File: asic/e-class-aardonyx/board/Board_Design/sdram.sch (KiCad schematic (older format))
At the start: 30 parts, among them J4 Conn_1x4, U15 SKT32E, U2 IS42S32160F-TSOP2, U3 CDCE913PW, Y2 27MHz

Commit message: updated compo placement
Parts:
- TP3, TP4: footprint TestPoint:TestPoint_Bridge_Pitch2.54mm_Drill0.7mm -> Connector_PinHeader_2.54mm:PinHeader_1x01_P2.54mm_Vertical
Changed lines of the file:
@@
 F 0 "TP3" V 10250 2888 50  0000 L CNN
 F 1 "TestPoint" V 10295 2888 50  0001 L CNN
-F 2 "TestPoint:TestPoint_Bridge_Pitch2.54mm_Drill0.7mm" H 10450 2700 50  0001 C CNN
+F 2 "Connector_PinHeader_2.54mm:PinHeader_1x01_P2.54mm_Vertical" H 10450 2700 50  0001 C CNN
 F 3 "~" H 10450 2700 50  0001 C CNN
 	1    10250 2700
@@
 F 0 "TP4" V 10250 2988 50  0000 L CNN
 F 1 "TestPoint" V 10295 2988 50  0001 L CNN
-F 2 "TestPoint:TestPoint_Bridge_Pitch2.54mm_Drill0.7mm" H 10450 2800 50  0001 C CNN
+F 2 "Connector_PinHeader_2.54mm:PinHeader_1x01_P2.54mm_Vertical" H 10450 2800 50  0001 C CNN
 F 3 "~" H 10450 2800 50  0001 C CNN
 	1    10250 2800

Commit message: add bom
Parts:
- R19, R20, R21, R22, R23: Digikey PartNumber 311-4.7KJRTR-ND -> 311-4.7KJRCT-ND
- U3: Description IC PROG PLL VCXO CLK SYN 14TSSOP -> IC PROG PLL VCXO CLK SYN 14TSSOP; Maufaturer Texas Instruments -> Texas Instruments
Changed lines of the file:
@@
 F 1 "4.7KE, 0402" V 7050 1900 50  0000 L CNN
 F 2 "Resistor_SMD:R_0402_1005Metric" V 7190 2190 50  0001 C CNN
-F 3 "https://www.digikey.in/product-detail/en/yageo/RC0402JR-074K7L/311-4-7KJRTR-ND/726477" H 7150 2200 50  0001 C CNN
+F 3 "https://www.digikey.in/product-detail/en/yageo/RC0402JR-074K7L/311-4-7KJRCT-ND/726477" H 7150 2200 50  0001 C CNN
 F 4 "RES SMD 4.7K OHM 5% 1/16W 0402" H 7150 2200 50  0001 C CNN "Description"
-F 5 "311-4.7KJRTR-ND" H 7150 2200 50  0001 C CNN "Digikey PartNumber"
+F 5 "311-4.7KJRCT-ND" H 7150 2200 50  0001 C CNN "Digikey PartNumber"
 F 6 "RC0402JR-074K7L" H 7150 2200 50  0001 C CNN "Manufactured Part Number"
 F 7 "Yageo" H 7150 2200 50  0001 C CNN "Maufaturer"
@@
 F 1 "4.7KE, 0402" V 6750 1900 50  0000 L CNN
 F 2 "Resistor_SMD:R_0402_1005Metric" V 6890 2190 50  0001 C CNN
-F 3 "https://www.digikey.in/product-detail/en/yageo/RC0402JR-074K7L/311-4-7KJRTR-ND/726477" H 6850 2200 50  0001 C CNN
+F 3 "https://www.digikey.in/product-detail/en/yageo/RC0402JR-074K7L/311-4-7KJRCT-ND/726477" H 6850 2200 50  0001 C CNN
 F 4 "RES SMD 4.7K OHM 5% 1/16W 0402" H 6850 2200 50  0001 C CNN "Description"
-F 5 "311-4.7KJRTR-ND" H 6850 2200 50  0001 C CNN "Digikey PartNumber"
+F 5 "311-4.7KJRCT-ND" H 6850 2200 50  0001 C CNN "Digikey PartNumber"
 F 6 "RC0402JR-074K7L" H 6850 2200 50  0001 C CNN "Manufactured Part Number"
 F 7 "Yageo" H 6850 2200 50  0001 C CNN "Maufaturer"
@@
 F 1 "4.7KE, 0402" V 7300 1900 50  0000 L CNN
 F 2 "Resistor_SMD:R_0402_1005Metric" V 7440 2190 50  0001 C CNN
-F 3 "https://www.digikey.in/product-detail/en/yageo/RC0402JR-074K7L/311-4-7KJRTR-ND/726477" H 7400 2200 50  0001 C CNN
+F 3 "https://www.digikey.in/product-detail/en/yageo/RC0402JR-074K7L/311-4-7KJRCT-ND/726477" H 7400 2200 50  0001 C CNN
 F 4 "RES SMD 4.7K OHM 5% 1/16W 0402" H 7400 2200 50  0001 C CNN "Description"
-F 5 "311-4.7KJRTR-ND" H 7400 2200 50  0001 C CNN "Digikey PartNumber"
+F 5 "311-4.7KJRCT-ND" H 7400 2200 50  0001 C CNN "Digikey PartNumber"
 F 6 "RC0402JR-074K7L" H 7400 2200 50  0001 C CNN "Manufactured Part Number"
 F 7 "Yageo" H 7400 2200 50  0001 C CNN "Maufaturer"
@@
 F 1 "4.7KE, 0402" H 7650 2700 50  0000 L CNN
 F 2 "Resistor_SMD:R_0402_1005Metric" V 7690 2790 50  0001 C CNN
-F 3 "https://www.digikey.in/product-detail/en/yageo/RC0402JR-074K7L/311-4-7KJRTR-ND/726477" H 7650 2800 50  0001 C CNN
+F 3 "https://www.digikey.in/product-detail/en/yageo/RC0402JR-074K7L/311-4-7KJRCT-ND/726477" H 7650 2800 50  0001 C CNN
 F 4 "NA" H 7750 2800 50  0000 C CNN "Field4"
 F 5 "RES SMD 4.7K OHM 5% 1/16W 0402" H 7650 2800 50  0001 C CNN "Description"
-F 6 "311-4.7KJRTR-ND" H 7650 2800 50  0001 C CNN "Digikey PartNumber"
+F 6 "311-4.7KJRCT-ND" H 7650 2800 50  0001 C CNN "Digikey PartNumber"
 F 7 "RC0402JR-074K7L" H 7650 2800 50  0001 C CNN "Manufactured Part Number"
 F 8 "Yageo" H 7650 2800 50  0001 C CNN "Maufaturer"
@@
 F 1 "4.7KE, 0402" H 7700 1950 50  0000 L CNN
 F 2 "Resistor_SMD:R_0402_1005Metric" V 7690 1990 50  0001 C CNN
-F 3 "https://www.digikey.in/product-detail/en/yageo/RC0402JR-074K7L/311-4-7KJRTR-ND/726477" H 7650 2000 50  0001 C CNN
+F 3 "https://www.digikey.in/product-detail/en/yageo/RC0402JR-074K7L/311-4-7KJRCT-ND/726477" H 7650 2000 50  0001 C CNN
 F 4 "NA" H 7750 2050 50  0000 C CNN "Field4"
 F 5 "RES SMD 4.7K OHM 5% 1/16W 0402" H 7650 2000 50  0001 C CNN "Description"
-F 6 "311-4.7KJRTR-ND" H 7650 2000 50  0001 C CNN "Digikey PartNumber"
+F 6 "311-4.7KJRCT-ND" H 7650 2000 50  0001 C CNN "Digikey PartNumber"
 F 7 "RC0402JR-074K7L" H 7650 2000 50  0001 C CNN "Manufactured Part Number"
 F 8 "Yageo" H 7650 2000 50  0001 C CNN "Maufaturer"
@@
 F 6 "Texas Instruments" H 8750 2200 50  0001 L BNN "Field6"
 F 7 "1543748" H 8750 2200 50  0001 L BNN "Field7"
-F 8 "	IC PROG PLL VCXO CLK SYN 14TSSOP" H 8750 2200 50  0001 C CNN "Description"
+F 8 "IC PROG PLL VCXO CLK SYN 14TSSOP" H 8750 2200 50  0001 C CNN "Description"
 F 9 "296-38908-1-ND" H 8750 2200 50  0001 C CNN "Digikey PartNumber"
 F 10 "CDCE913PWR" H 8750 2200 50  0001 C CNN "Manufactured Part Number"
-F 11 "	Texas Instruments" H 8750 2200 50  0001 C CNN "Maufaturer"
+F 11 "Texas Instruments" H 8750 2200 50  0001 C CNN "Maufaturer"
 	1    8750 2200
 	1    0    0    -1

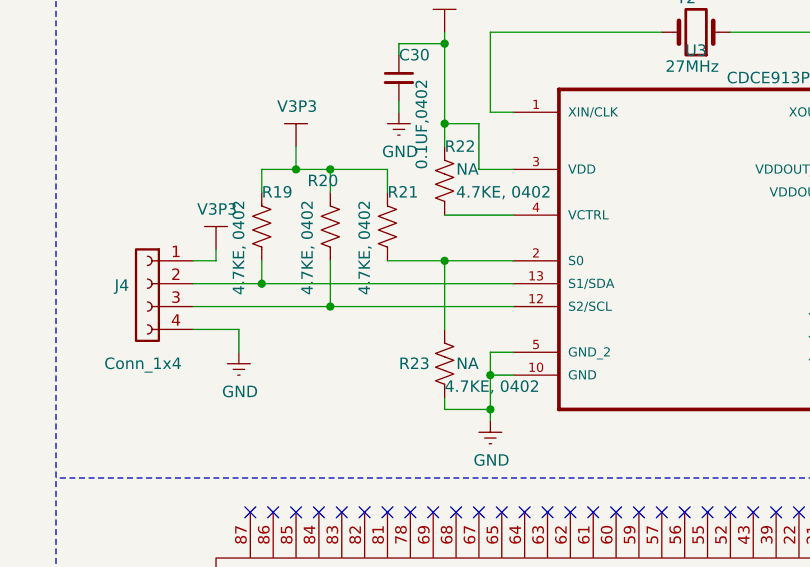
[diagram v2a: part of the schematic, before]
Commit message: Replacing ADM1085 with ADM1186
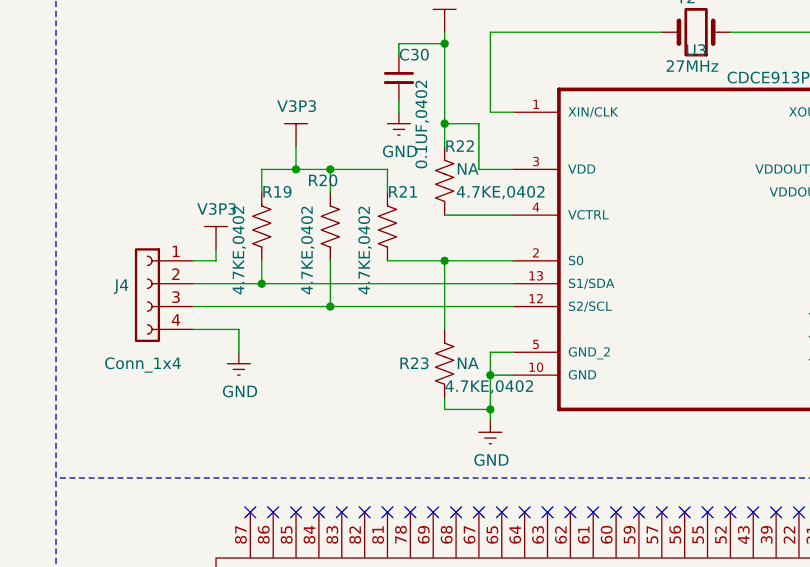
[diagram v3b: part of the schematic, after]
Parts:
- R19, R20, R21, R22, R23: value 4.7KE, 0402 -> 4.7KE,0402
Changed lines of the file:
@@
 AR Path="/5D8B37B8/5EFB4D01" Ref="R20"  Part="1"
 F 0 "R20" H 7050 2400 50  0000 L CNN
-F 1 "4.7KE, 0402" V 7050 1900 50  0000 L CNN
+F 1 "4.7KE,0402" V 7050 1900 50  0000 L CNN
 F 2 "Resistor_SMD:R_0402_1005Metric" V 7190 2190 50  0001 C CNN
 F 3 "https://www.digikey.in/product-detail/en/yageo/RC0402JR-074K7L/311-4-7KJRCT-ND/726477" H 7150 2200 50  0001 C CNN
@@
 AR Path="/5D8B37B8/5EFB4D07" Ref="R19"  Part="1"
 F 0 "R19" H 6850 2350 50  0000 L CNN
-F 1 "4.7KE, 0402" V 6750 1900 50  0000 L CNN
+F 1 "4.7KE,0402" V 6750 1900 50  0000 L CNN
 F 2 "Resistor_SMD:R_0402_1005Metric" V 6890 2190 50  0001 C CNN
 F 3 "https://www.digikey.in/product-detail/en/yageo/RC0402JR-074K7L/311-4-7KJRCT-ND/726477" H 6850 2200 50  0001 C CNN
@@
 AR Path="/5D8B37B8/5F80E136" Ref="R21"  Part="1"
 F 0 "R21" H 7400 2350 50  0000 L CNN
-F 1 "4.7KE, 0402" V 7300 1900 50  0000 L CNN
+F 1 "4.7KE,0402" V 7300 1900 50  0000 L CNN
 F 2 "Resistor_SMD:R_0402_1005Metric" V 7440 2190 50  0001 C CNN
 F 3 "https://www.digikey.in/product-detail/en/yageo/RC0402JR-074K7L/311-4-7KJRCT-ND/726477" H 7400 2200 50  0001 C CNN
@@
 AR Path="/5D8B37B8/5F82D0FE" Ref="R23"  Part="1"
 F 0 "R23" H 7450 2800 50  0000 L CNN
-F 1 "4.7KE, 0402" H 7650 2700 50  0000 L CNN
+F 1 "4.7KE,0402" H 7650 2700 50  0000 L CNN
 F 2 "Resistor_SMD:R_0402_1005Metric" V 7690 2790 50  0001 C CNN
 F 3 "https://www.digikey.in/product-detail/en/yageo/RC0402JR-074K7L/311-4-7KJRCT-ND/726477" H 7650 2800 50  0001 C CNN
@@
 AR Path="/5D8B37B8/5F8A4363" Ref="R22"  Part="1"
 F 0 "R22" H 7650 2150 50  0000 L CNN
-F 1 "4.7KE, 0402" H 7700 1950 50  0000 L CNN
+F 1 "4.7KE,0402" H 7700 1950 50  0000 L CNN
 F 2 "Resistor_SMD:R_0402_1005Metric" V 7690 1990 50  0001 C CNN
 F 3 "https://www.digikey.in/product-detail/en/yageo/RC0402JR-074K7L/311-4-7KJRCT-ND/726477" H 7650 2000 50  0001 C CNN

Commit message: Updating footprint for test points
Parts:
- TP3, TP4: footprint Connector_PinHeader_2.54mm:PinHeader_1x01_P2.54mm_Vertical -> TestPoint:TestPoint_Pad_D1.5mm
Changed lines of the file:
@@
 F 0 "TP3" V 10250 2888 50  0000 L CNN
 F 1 "TestPoint" V 10295 2888 50  0001 L CNN
-F 2 "Connector_PinHeader_2.54mm:PinHeader_1x01_P2.54mm_Vertical" H 10450 2700 50  0001 C CNN
+F 2 "TestPoint:TestPoint_Pad_D1.5mm" H 10450 2700 50  0001 C CNN
 F 3 "~" H 10450 2700 50  0001 C CNN
 	1    10250 2700
@@
 F 0 "TP4" V 10250 2988 50  0000 L CNN
 F 1 "TestPoint" V 10295 2988 50  0001 L CNN
-F 2 "Connector_PinHeader_2.54mm:PinHeader_1x01_P2.54mm_Vertical" H 10450 2800 50  0001 C CNN
+F 2 "TestPoint:TestPoint_Pad_D1.5mm" H 10450 2800 50  0001 C CNN
 F 3 "~" H 10450 2800 50  0001 C CNN
 	1    10250 2800

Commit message: Updating placements
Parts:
- TP3, TP4: footprint TestPoint:TestPoint_Pad_D1.5mm -> TestPoint:TestPoint_Pad_D1.0mm
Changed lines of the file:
@@
 F 0 "TP3" V 10250 2888 50  0000 L CNN
 F 1 "TestPoint" V 10295 2888 50  0001 L CNN
-F 2 "TestPoint:TestPoint_Pad_D1.5mm" H 10450 2700 50  0001 C CNN
+F 2 "TestPoint:TestPoint_Pad_D1.0mm" H 10450 2700 50  0001 C CNN
 F 3 "~" H 10450 2700 50  0001 C CNN
 	1    10250 2700
@@
 F 0 "TP4" V 10250 2988 50  0000 L CNN
 F 1 "TestPoint" V 10295 2988 50  0001 L CNN
-F 2 "TestPoint:TestPoint_Pad_D1.5mm" H 10450 2800 50  0001 C CNN
+F 2 "TestPoint:TestPoint_Pad_D1.0mm" H 10450 2800 50  0001 C CNN
 F 3 "~" H 10450 2800 50  0001 C CNN
 	1    10250 2800

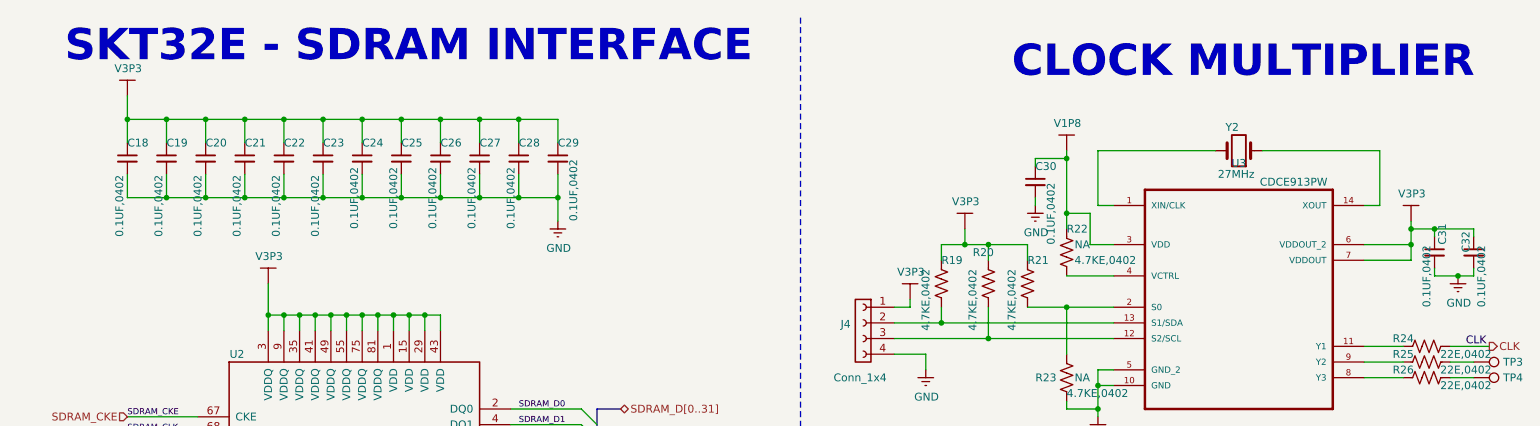
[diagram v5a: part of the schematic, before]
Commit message: Updating 1x6 connector
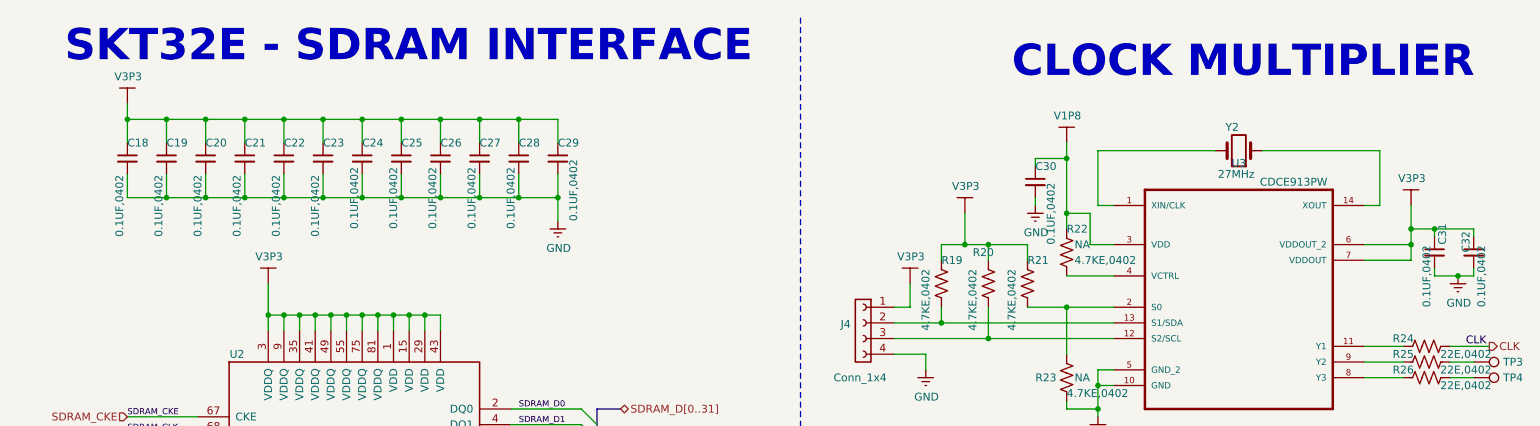
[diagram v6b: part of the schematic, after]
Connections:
- net V1P8: now reaches C30.1, R22.1, U3.3 (VDD)
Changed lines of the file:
@@
 EESchema Schematic File Version 4
-EELAYER 30 0
+LIBS:Aardonyx-cache
+EELAYER 29 0
 EELAYER END
 $Descr A4 11693 8268
@@
 Wire Wire Line
 	2650 2400 2750 2400
-Wire Wire Line
-	2550 2400 2550 2200
 Connection ~ 2550 2400
 Wire Wire Line
@@
 Wire Wire Line
 	4150 1650 4400 1650
-Wire Wire Line
-	1650 1150 1650 1000
 Connection ~ 1650 1150
 Wire Wire Line
@@
 SDRAM_CKE
 $Comp
-L Aardonyx-rescue:V3P3-aardonyx #PWR024
-U 1 1 5DC441F1
-P 1650 1000
-F 0 "#PWR024" H 1800 950 50  0001 C CNN
-F 1 "V3P3" H 1655 1175 50  0000 C CNN
-F 2 "" H 1650 1000 50  0001 C CNN
-F 3 "" H 1650 1000 50  0001 C CNN
-	1    1650 1000
-	1    0    0    -1
-$EndComp
-$Comp
-L Aardonyx-rescue:V3P3-aardonyx #PWR025
-U 1 1 5DC4BA51
-P 2550 2200
-F 0 "#PWR025" H 2700 2150 50  0001 C CNN
-F 1 "V3P3" H 2555 2375 50  0000 C CNN
-F 2 "" H 2550 2200 50  0001 C CNN
-F 3 "" H 2550 2200 50  0001 C CNN
-	1    2550 2200
-	1    0    0    -1
-$EndComp
-$Comp
 L Aardonyx-rescue:GND-aardonyx #PWR026
 U 1 1 5DC6067F
@@
 F 3 "" H 7850 3050 50  0001 C CNN
 	1    7850 3050
-	1    0    0    -1
-$EndComp
-$Comp
-L Aardonyx-rescue:V3P3-aardonyx #PWR?
-U 1 1 5EFB4CFB
-P 9850 1800
-AR Path="/5D8B3740/5EFB4CFB" Ref="#PWR?"  Part="1"
-AR Path="/5D8B37B8/5EFB4CFB" Ref="#PWR034"  Part="1"
-F 0 "#PWR034" H 10000 1750 50  0001 C CNN
-F 1 "V3P3" H 9855 1975 50  0000 C CNN
-F 2 "" H 9850 1800 50  0001 C CNN
-F 3 "" H 9850 1800 50  0001 C CNN
-	1    9850 1800
 	1    0    0    -1
 $EndComp
@@
 Wire Wire Line
 	9550 2600 9800 2600
-$Comp
-L Aardonyx-rescue:V3P3-aardonyx #PWR?
-U 1 1 5EFB4D20
-P 7000 1850
-AR Path="/5D8B3740/5EFB4D20" Ref="#PWR?"  Part="1"
-AR Path="/5D8B37B8/5EFB4D20" Ref="#PWR030"  Part="1"
-F 0 "#PWR030" H 7150 1800 50  0001 C CNN
-F 1 "V3P3" H 7005 2025 50  0000 C CNN
-F 2 "" H 7000 1850 50  0001 C CNN
-F 3 "" H 7000 1850 50  0001 C CNN
-	1    7000 1850
-	1    0    0    -1
-$EndComp
 Wire Wire Line
 	6850 1950 7000 1950
-Wire Wire Line
-	7000 1950 7000 1850
 Wire Wire Line
 	7000 1950 7150 1950
@@
 Wire Wire Line
 	9550 1950 9850 1950
-Wire Wire Line
-	9850 1800 9850 1850
 Wire Wire Line
 	9850 1950 9850 2050
@@
 	10250 2150 10250 2100
 Connection ~ 10150 2150
-$Comp
-L Aardonyx-rescue:V3P3-aardonyx #PWR?
-U 1 1 5EFB4D70
-P 6650 2300
-AR Path="/5D8B3740/5EFB4D70" Ref="#PWR?"  Part="1"
-AR Path="/5D8B37B8/5EFB4D70" Ref="#PWR028"  Part="1"
-F 0 "#PWR028" H 6800 2250 50  0001 C CNN
-F 1 "V3P3" H 6655 2475 50  0000 C CNN
-F 2 "" H 6650 2300 50  0001 C CNN
-F 3 "" H 6650 2300 50  0001 C CNN
-	1    6650 2300
-	1    0    0    -1
-$EndComp
-Wire Wire Line
-	6650 2300 6650 2350
 Wire Wire Line
 	6650 2350 6550 2350
@@
 	1    0    0    -1
 $EndComp
-Connection ~ 7650 1400
 Wire Wire Line
 	7450 1400 7450 1450
 Wire Wire Line
 	7650 1400 7450 1400
-Wire Wire Line
-	7650 1350 7650 1400
 $Comp
 L Aardonyx-rescue:C_Small-aardonyx C?
@@
 	0    1    1    0
 $EndComp
-$Comp
-L Aardonyx-rescue:V1P8-skt32e_asic #PWR0140
-U 1 1 5ED7320E
-P 7650 1350
-F 0 "#PWR0140" H 7800 1300 50  0001 C CNN
-F 1 "V1P8" H 7655 1525 50  0000 C CNN
-F 2 "" H 7650 1350 50  0001 C CNN
-F 3 "" H 7650 1350 50  0001 C CNN
-	1    7650 1350
-	1    0    0    -1
-$EndComp
 Wire Notes Line
 	11200 3300 5950 3300
@@
 Text Notes 4250 7100 0    50   ~ 0
 86-pin TSOP-ll
+$Comp
+L Aardonyx-rescue:V3P3 #PWR?
+U 1 1 5F10B8C3
+P 1650 1050
+AR Path="/5D8B3761/5F10B8C3" Ref="#PWR?"  Part="1"
+AR Path="/5D8B37B8/5F10B8C3" Ref="#PWR0133"  Part="1"
+F 0 "#PWR0133" H 1800 1000 50  0001 C CNN
+F 1 "V3P3" H 1655 1223 50  0000 C CNN
+F 2 "" H 1650 1050 50  0001 C CNN
+F 3 "" H 1650 1050 50  0001 C CNN
+	1    1650 1050
+	1    0    0    -1
+$EndComp
+Wire Wire Line
+	1650 1050 1650 1150
+$Comp
+L Aardonyx-rescue:V3P3 #PWR?
+U 1 1 5F1273CB
+P 2550 2200
+AR Path="/5D8B3761/5F1273CB" Ref="#PWR?"  Part="1"
+AR Path="/5D8B37B8/5F1273CB" Ref="#PWR0134"  Part="1"
+F 0 "#PWR0134" H 2700 2150 50  0001 C CNN
+F 1 "V3P3" H 2555 2373 50  0000 C CNN
+F 2 "" H 2550 2200 50  0001 C CNN
+F 3 "" H 2550 2200 50  0001 C CNN
+	1    2550 2200
+	1    0    0    -1
+$EndComp
+Wire Wire Line
+	2550 2200 2550 2400
+$Comp
+L Aardonyx-rescue:V3P3 #PWR?
+U 1 1 5F135917
+P 9850 1700
+AR Path="/5D8B3761/5F135917" Ref="#PWR?"  Part="1"
+AR Path="/5D8B37B8/5F135917" Ref="#PWR0135"  Part="1"
+F 0 "#PWR0135" H 10000 1650 50  0001 C CNN
+F 1 "V3P3" H 9855 1873 50  0000 C CNN
+F 2 "" H 9850 1700 50  0001 C CNN
+F 3 "" H 9850 1700 50  0001 C CNN
+	1    9850 1700
+	1    0    0    -1
+$EndComp
+Wire Wire Line
+	9850 1700 9850 1850
+$Comp
+L Aardonyx-rescue:V3P3 #PWR?
+U 1 1 5F142818
+P 7000 1750
+AR Path="/5D8B3761/5F142818" Ref="#PWR?"  Part="1"
+AR Path="/5D8B37B8/5F142818" Ref="#PWR0136"  Part="1"
+F 0 "#PWR0136" H 7150 1700 50  0001 C CNN
+F 1 "V3P3" H 7005 1923 50  0000 C CNN
+F 2 "" H 7000 1750 50  0001 C CNN
+F 3 "" H 7000 1750 50  0001 C CNN
+	1    7000 1750
+	1    0    0    -1
+$EndComp
+Wire Wire Line
+	7000 1750 7000 1950
+$Comp
+L Aardonyx-rescue:V3P3 #PWR?
+U 1 1 5F14ED8D
+P 6650 2200
+AR Path="/5D8B3761/5F14ED8D" Ref="#PWR?"  Part="1"
+AR Path="/5D8B37B8/5F14ED8D" Ref="#PWR0140"  Part="1"
+F 0 "#PWR0140" H 6800 2150 50  0001 C CNN
+F 1 "V3P3" H 6655 2373 50  0000 C CNN
+F 2 "" H 6650 2200 50  0001 C CNN
+F 3 "" H 6650 2200 50  0001 C CNN
+	1    6650 2200
+	1    0    0    -1
+$EndComp
+Wire Wire Line
+	6650 2200 6650 2350
+$Comp
+L Aardonyx-rescue:V1P8 #PWR0156
+U 1 1 5F4938CA
+P 7650 1300
+F 0 "#PWR0156" H 7800 1250 50  0001 C CNN
+F 1 "V1P8" H 7655 1473 50  0000 C CNN
+F 2 "" H 7650 1300 50  0001 C CNN
+F 3 "" H 7650 1300 50  0001 C CNN
+	1    7650 1300
+	1    0    0    -1
+$EndComp
+Wire Wire Line
+	7650 1400 7650 1300
 Wire Bus Line
 	1550 5700 1550 6100
@@
 Wire Bus Line
 	4650 3000 4650 6600
+Connection ~ 7650 1400
 $EndSCHEMATC
